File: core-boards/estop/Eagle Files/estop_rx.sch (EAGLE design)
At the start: 29 parts, among them J1 RFM95W-3072, J2 JST-XH-02-PIN-ROUND-PAD, J3 B2PS-VH(LF)(SN), U1 R-78E5.0-1.0CONV_R-78E5.0-1.0, U4 ATMEGA328P-AUR, X6 B6B-EH-A(LF)(SN)

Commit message: estop tx design review
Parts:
- added R1: 10k, rcl:R-US_R0603
- J2: value JST-XH-02-PIN-ROUND-PAD -> B2PS-VH(LF)(SN); device IGVC-Connector:JST-XH-02-PIN-ROUND-PAD -> RoboJackets-Connectors:B2PS-VH(LF)(SN)
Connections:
- net GND: now also J2.2, R1.1; no longer J1.RST, J2-2.S
- net N$1: now also J2.1; no longer J2-1.S
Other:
- moved on the sheet: C6, R2, S3

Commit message: final tm edits for design review
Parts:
- removed JP2: Serial, pinhead:PINHD-1X3
- added C7: 0.1uF, rcl:C-USC0603
- added U2: MCP2551T-E/SN, IGVC-Microcontroller:MCP2551T-E/SN
- added X1: JST-XH-03-PIN-ROUND-PAD, IGVC-Connector:JST-XH-03-PIN-ROUND-PAD
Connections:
- removed net RX: JP2.2, U4.PD0_(RXD/PCINT16)
- removed net TX: JP2.1, U4.PD1_(TXD/PCINT17)
- new net CAN_N: U2.CANL, X1-2.S
- new net CAN_P: U2.CANH, X1-3.S
- new net CAN_RX: U2.RXD, U4.PD0_(RXD/PCINT16)
- new net CAN_TX: U2.TXD, U4.PD1_(TXD/PCINT17)
- new net N$5: J1.RST, R1.2
- net +5V: now also C7.1, U2.VDD, X1-1.S
- net CE: now also U4.(PCINT2/SS/OC1B)_PB2; no longer U4.(PCINT6/XTAL1/TOSC1)_PB6
- net GND: now also C7.2, U2.RS, U2.VSS; no longer JP2.3
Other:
- note added: "CAN Bus"
- note added: "E-Stop Signal In"
- note added: "Relay"
- note removed: "24V Button IN"
- note removed: "24V OUT"
- moved on the sheet: C1, C5, J2, J3, R1, R10, R3, R9, U1, X6

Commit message: almost order ready haha
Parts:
- removed X1: JST-XH-03-PIN-ROUND-PAD, IGVC-Connector:JST-XH-03-PIN-ROUND-PAD
- removed X6: B6B-EH-A(LF)(SN), IGVC-Connector:B6B-EH-A(LF)(SN)
- added J4: 2-PIN_2MM-V, RoboJackets-Connectors:2-PIN_2MM-V
- added J5: 6-PIN_2MM-V, RoboJackets-Connectors:6-PIN_2MM-V
- added R7: 10k, rcl:R-US_R0603
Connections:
- new net EN: U4.(PCINT23/AIN1)_PD7
- new net N$6: J1.EN, R7.2
- net +24V: now also J5.1; no longer X6.X-1
- net +5V: now also R7.1; no longer X1-1.S
- net CAN_N: now also J4.2; no longer X1-2.S
- net CAN_P: now also J4.1; no longer X1-3.S
- net DIODE_TO_GREEN: now also J5.2; no longer X6.X-2
- net DIODE_TO_INTER: now also J5.4; no longer X6.X-4
- net GND: now also J5.6; no longer X6.X-6
- net MOTOR_POWER: now also J5.3; no longer X6.X-3
- net SOLENOID_TRIG: now also J5.5; no longer X6.X-5

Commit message: things should be done tm
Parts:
- added U6: D5V0L1B2WS-7, IGVC-Discrete:D5V0L1B2WS-7
- C1, C5: device rcl:C-USC0603 -> rcl:C-USC0805
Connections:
- net +12V: now also U6.EPAD_2
- net GND: now also U6.EPAD
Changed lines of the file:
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@@
 <part name="P+7" library="supply1" library_urn="urn:adsk.eagle:library:371" deviceset="+5V" device=""/>
 <part name="U1" library="IGVC-Regulator" deviceset="R-78E5.0-1.0" device="CONV_R-78E5.0-1.0"/>
-<part name="C1" library="rcl" library_urn="urn:adsk.eagle:library:334" deviceset="C-US" device="C0603" package3d_urn="urn:adsk.eagle:package:23616/2" value="10uF"/>
+<part name="C1" library="rcl" library_urn="urn:adsk.eagle:library:334" deviceset="C-US" device="C0805" package3d_urn="urn:adsk.eagle:package:23617/2" value="10uF"/>
 <part name="P+9" library="supply1" library_urn="urn:adsk.eagle:library:371" deviceset="+12V" device=""/>
 <part name="GND8" library="supply1" library_urn="urn:adsk.eagle:library:371" deviceset="GND" device=""/>
@@
 <part name="C7" library="rcl" library_urn="urn:adsk.eagle:library:334" deviceset="C-US" device="C0603" package3d_urn="urn:adsk.eagle:package:23616/2" value="0.1uF"/>
 <part name="P+12" library="supply1" library_urn="urn:adsk.eagle:library:371" deviceset="+5V" device=""/>
-<part name="C5" library="rcl" library_urn="urn:adsk.eagle:library:334" deviceset="C-US" device="C0603" package3d_urn="urn:adsk.eagle:package:23616/2" value="10uF"/>
+<part name="C5" library="rcl" library_urn="urn:adsk.eagle:library:334" deviceset="C-US" device="C0805" package3d_urn="urn:adsk.eagle:package:23617/2" value="10uF"/>
 <part name="P+3" library="supply1" library_urn="urn:adsk.eagle:library:371" deviceset="+5V" device=""/>
 <part name="P+8" library="supply1" library_urn="urn:adsk.eagle:library:371" deviceset="+5V" device=""/>
@@
 <part name="R7" library="rcl" library_urn="urn:adsk.eagle:library:334" deviceset="R-US_" device="R0603" package3d_urn="urn:adsk.eagle:package:23555/3" value="10k"/>
 <part name="P+1" library="supply1" library_urn="urn:adsk.eagle:library:371" deviceset="+5V" device=""/>
+<part name="U6" library="IGVC-Discrete" deviceset="D5V0L1B2WS-7" device=""/>
+<part name="GND1" library="supply1" library_urn="urn:adsk.eagle:library:371" deviceset="GND" device=""/>
+<part name="P+14" library="supply1" library_urn="urn:adsk.eagle:library:371" deviceset="+12V" device=""/>
 </parts>
 <sheets>
@@
 <attribute name="VALUE" x="261.62" y="391.16" size="1.778" layer="96" rot="R90"/>
 </instance>
+<instance part="U6" gate="A" x="375.92" y="347.98" smashed="yes">
+<attribute name="NAME" x="383.3876" y="355.5746" size="2.0828" layer="95" ratio="6" rot="SR0"/>
+<attribute name="VALUE" x="383.5146" y="353.2886" size="2.0828" layer="96" ratio="6" rot="SR0"/>
+</instance>
+<instance part="GND1" gate="1" x="414.02" y="342.9" smashed="yes">
+<attribute name="VALUE" x="411.48" y="340.36" size="1.778" layer="96"/>
+</instance>
+<instance part="P+14" gate="1" x="378.46" y="355.6" smashed="yes">
+<attribute name="VALUE" x="375.92" y="350.52" size="1.778" layer="96" rot="R90"/>
+</instance>
 </instances>
 <busses>
@@
 <pinref part="GND13" gate="1" pin="GND"/>
 </segment>
+<segment>
+<pinref part="U6" gate="A" pin="EPAD"/>
+<wire x1="408.94" y1="347.98" x2="414.02" y2="347.98" width="0.1524" layer="91"/>
+<wire x1="414.02" y1="347.98" x2="414.02" y2="345.44" width="0.1524" layer="91"/>
+<pinref part="GND1" gate="1" pin="GND"/>
+</segment>
 </net>
 <net name="MISO" class="0">
@@
 <pinref part="P+10" gate="1" pin="+12V"/>
 </segment>
-</net>
+<segment>
+<pinref part="U6" gate="A" pin="EPAD_2"/>
+<wire x1="378.46" y1="347.98" x2="378.46" y2="353.06" width="0.1524" layer="91"/>
+<pinref part="P+14" gate="1" pin="+12V"/>
+</segment>
+</net>

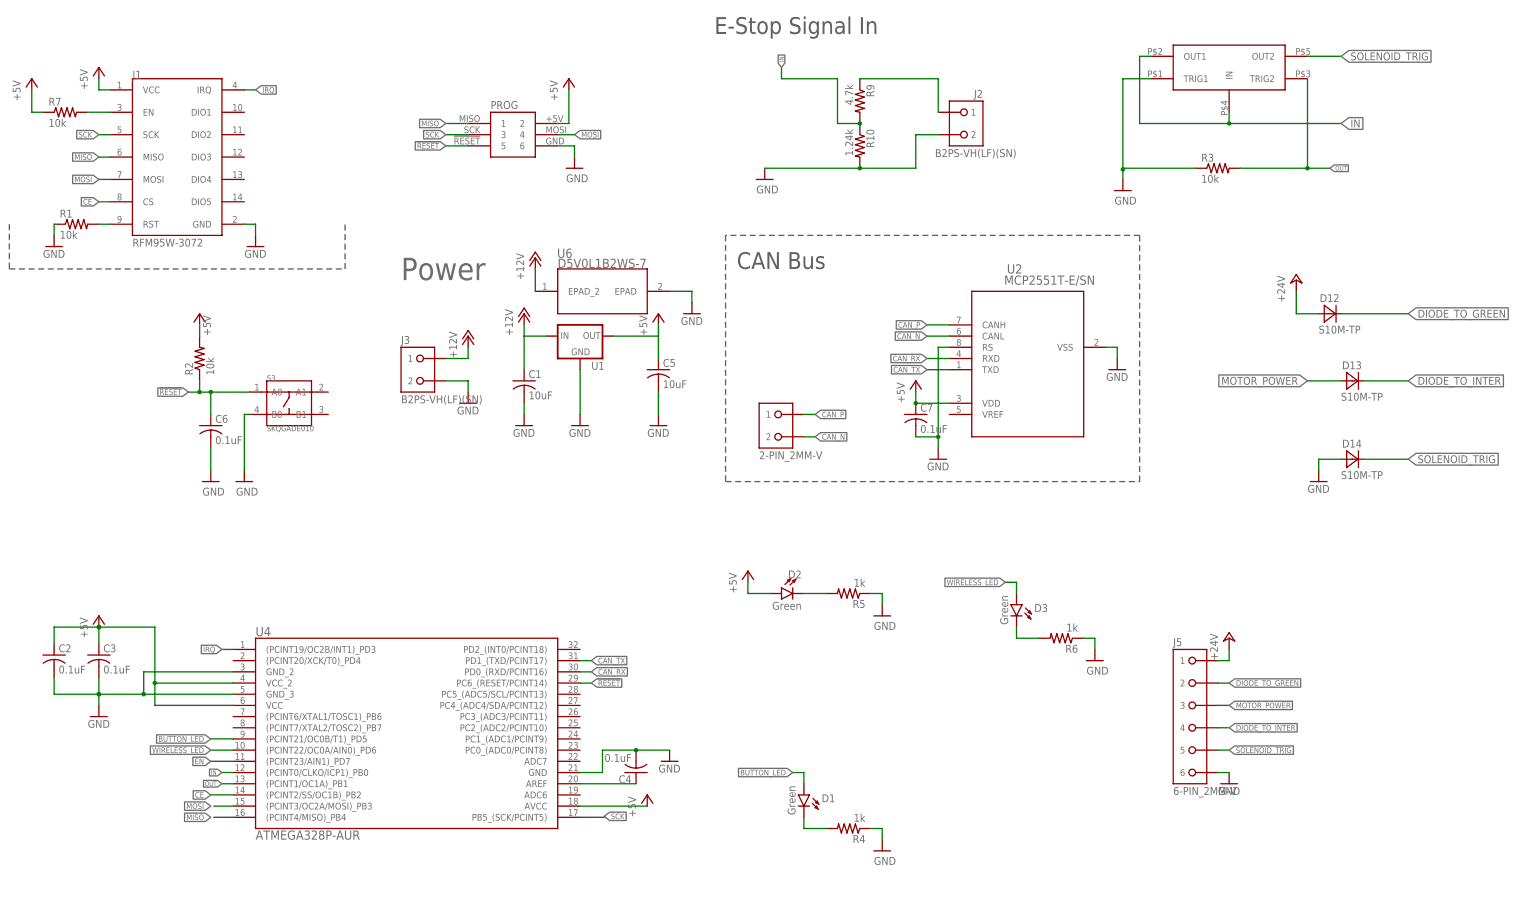
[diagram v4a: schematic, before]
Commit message: Fixed estop RX
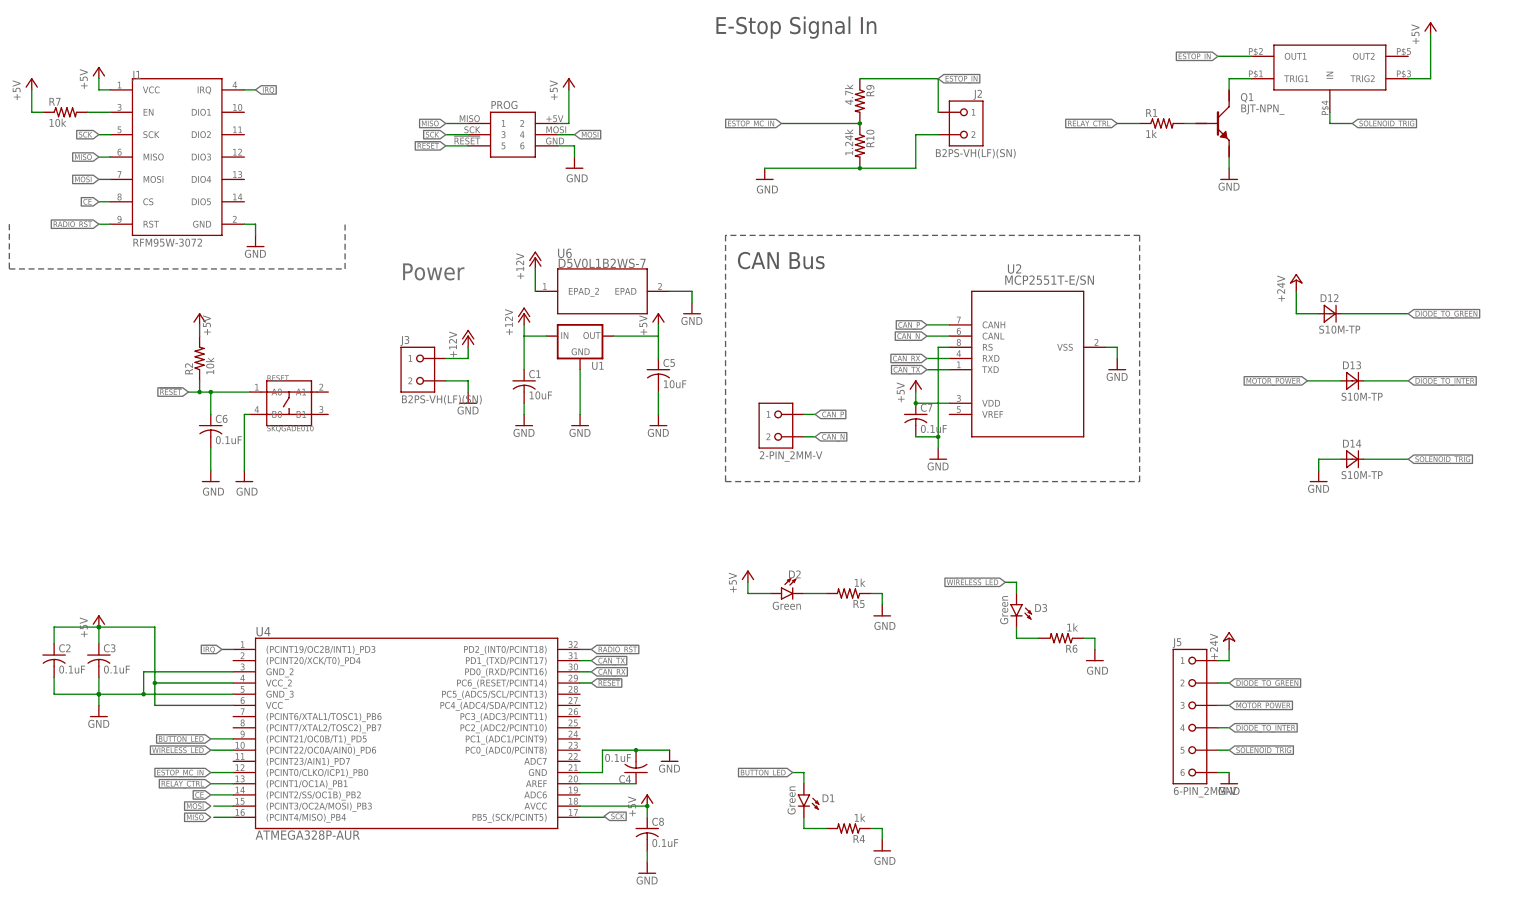
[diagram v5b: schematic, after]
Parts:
- removed R3: 10k, resistor:R-US_R0603
- added C8: 0.1uF, rcl:C-USC0603
- added Q1: BJT-NPN_, RoboJackets-Discrete:BJT-NPN_
- R1: value 10k -> 1k
- renumbered S3 to RESET
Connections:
- removed net EN: U4.(PCINT23/AIN1)_PD7
- removed net IN: R10.1, R9.2, U$1.IN, U$1.OUT1, U4.(PCINT0/CLKO/ICP1)_PB0
- removed net OUT: R3.2, U$1.TRIG2, U4.(PCINT1/OC1A)_PB1
- new net ESTOP_IN: J2.1, R9.1, U$1.OUT1
- new net ESTOP_MC_IN: R10.1, R9.2, U4.(PCINT0/CLKO/ICP1)_PB0
- new net RADIO_RST: J1.RST, U4.PD2_(INT0/PCINT18)
- new net RELAY_CTRL: R1.1, U4.(PCINT1/OC1A)_PB1
- net +5V: now also C8.1, U$1.TRIG2
- net GND: now also C8.2, Q1.E; no longer R1.1, R3.1, U$1.TRIG1
- net N$1: now also Q1.C, U$1.TRIG1; no longer J2.1, R9.1
- net N$5: now also Q1.B; no longer J1.RST
- net SOLENOID_TRIG: now also U$1.IN; no longer U$1.OUT2
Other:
- note removed: "Import Symbol"
- moved on the sheet: R1

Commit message: estop rx CAN controller added
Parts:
- added C10, C9: 22pF, SparkFun-Capacitors:22PF-50V-5%(0603)
- added C11: 0.1uF, SparkFun-Capacitors:0.1UF-25V(+80/-20%)(0603)
- added Q2: 16MHz, SparkFun-FreqCtrl:CRYSTAL5X3
- added R3: 10k, resistor:R-US_R0603
- added U3: MCP2515, SparkFun-DigitalIC:MCP2510SO
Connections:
- removed net CAN_RX: U2.RXD, U4.PD0_(RXD/PCINT16)
- removed net CAN_TX: U2.TXD, U4.PD1_(TXD/PCINT17)
- new net CAN_CS: R3.2, U3>NAME.CS, U4.(PCINT23/AIN1)_PD7
- new net CAN_INT: U3>NAME.INT, U4.(PCINT20/XCK/T0)_PD4
- new net CAN_RXD: U2.RXD, U3>NAME.RXCAN
- new net CAN_TXD: U2.TXD, U3>NAME.TXCAN
- new net N$17: C10.2, Q2.2, U3>NAME.OSC1
- new net N$18: C9.2, Q2.1, U3>NAME.OSC2
- net !RESET: now also U3>NAME.RESET
- net +5V: now also C11.2, R3.1, U3P.VDD
- net GND: now also C10.1, C11.1, C9.1, U3P.VSS
- net MISO: now also U3>NAME.SO
- net MOSI: now also U3>NAME.SI
- net SCK: now also U3>NAME.SCK
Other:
- note added: "CAN Controller"
